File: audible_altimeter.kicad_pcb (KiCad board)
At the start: 2 copper layers, 52.4 x 29.3 mm, 77 parts, among them CON1 BUQ2-USB-MICRO-B, IC1 BUQ2-ATXMEGA128A4U-A, P1 CONN_2, Q1 NPN, SW1 SW_LEFT, SW2 SW_DOWN, SW3 SW_UP, SW4 SW_CENTER, SW5 SW_RIGHT, U1 MCP7940M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

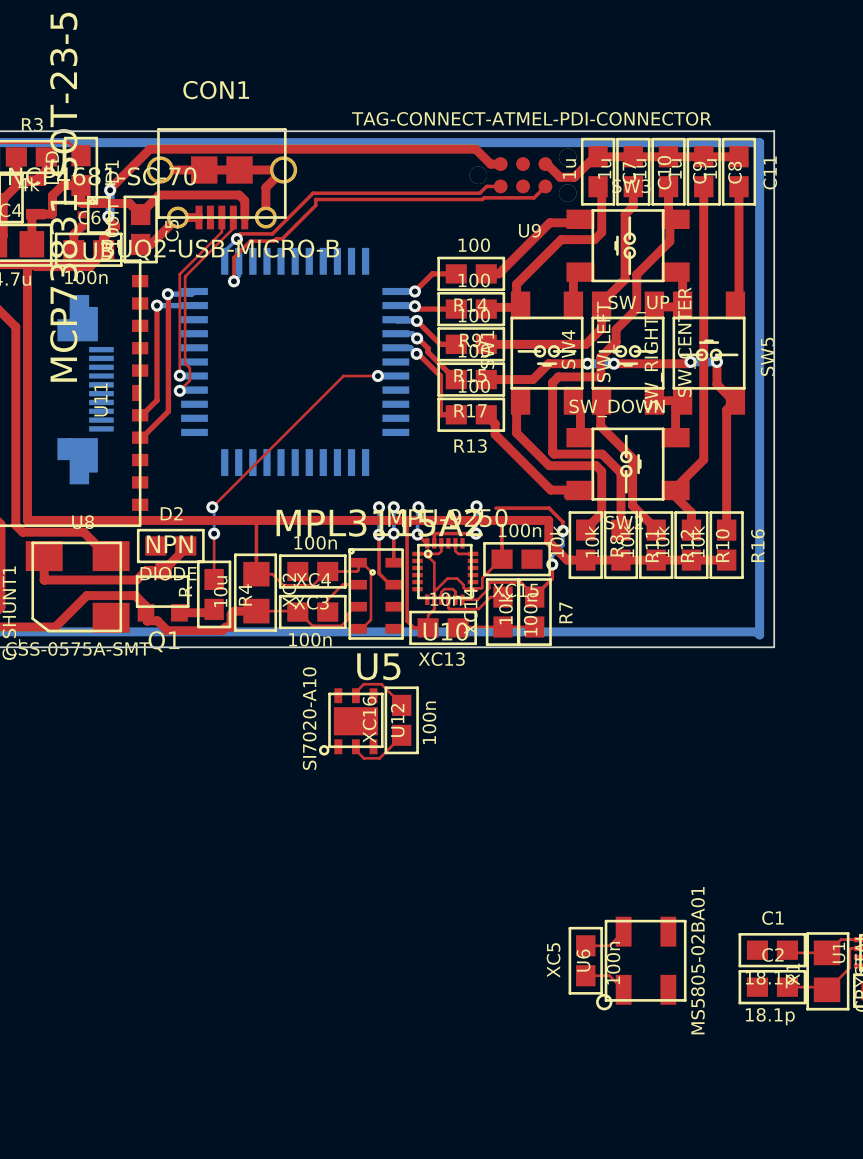
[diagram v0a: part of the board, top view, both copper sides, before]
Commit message: Before making larger board. - Changed GPS module
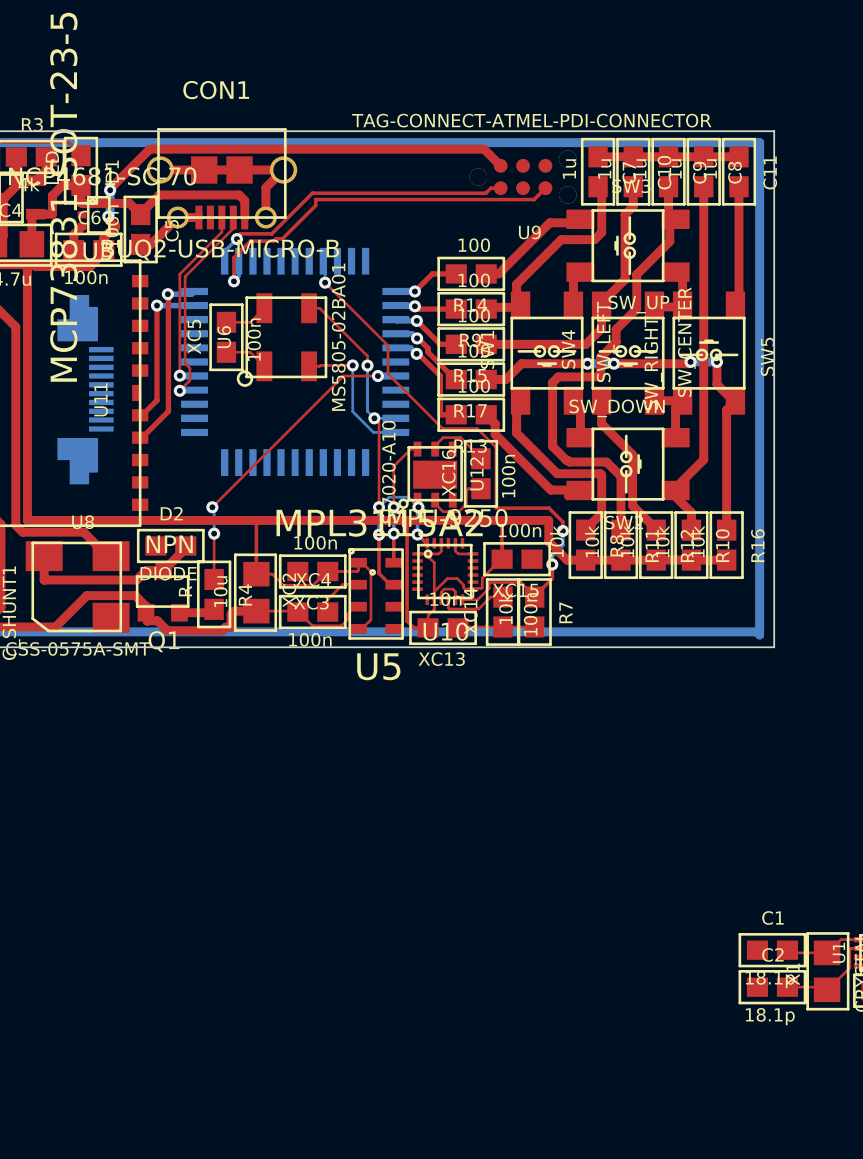
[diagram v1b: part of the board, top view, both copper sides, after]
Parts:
- moved XC5 40.9 mm to (120.9, 34.1)
- moved U6 40.9 mm to (124.3, 34.1)
- moved U12 14.7 mm to (132.8, 42.0)
- moved XC16 14.7 mm to (135.3, 41.9)
- moved U9 0.10 mm to (135.2, 25.0)
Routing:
- net /MCU/ACCELERATOR_INT: track 14.0 -> 33.3 mm, vias 2 -> 3
- net /9-Axis/I2C_SDA: track 7.19 -> 24.4 mm, vias 4 -> 6
- net /9-Axis/I2C_SCL: track 7.61 -> 15.3 mm, vias 4 -> 3
- net GND: track 265.7 -> 262.6 mm

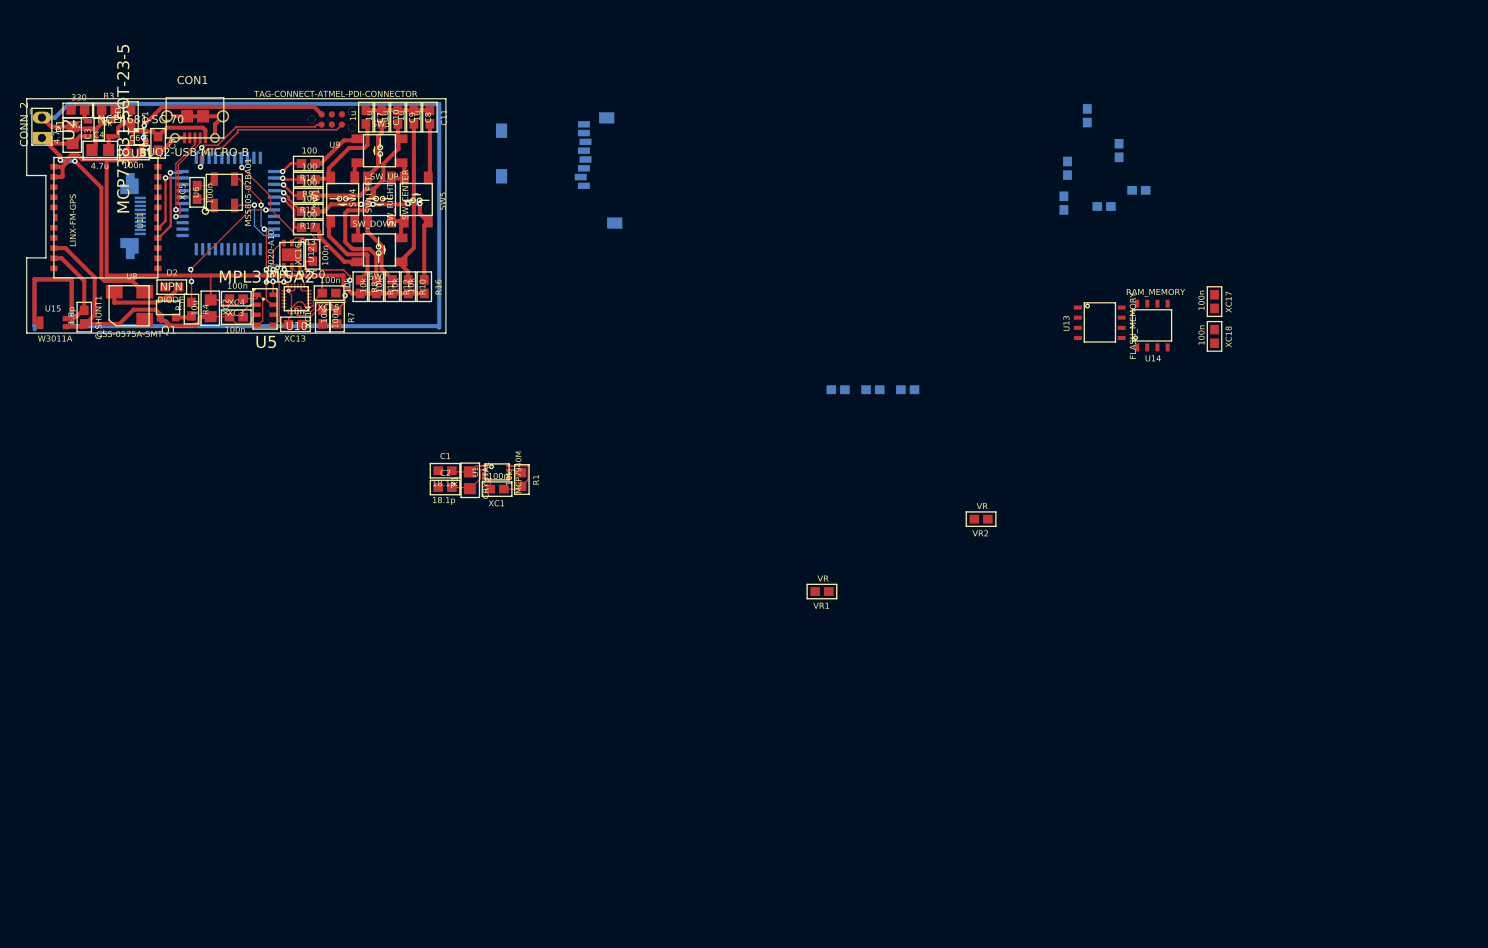
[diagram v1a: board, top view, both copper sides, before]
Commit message: Before adding proper reset and battery monitor
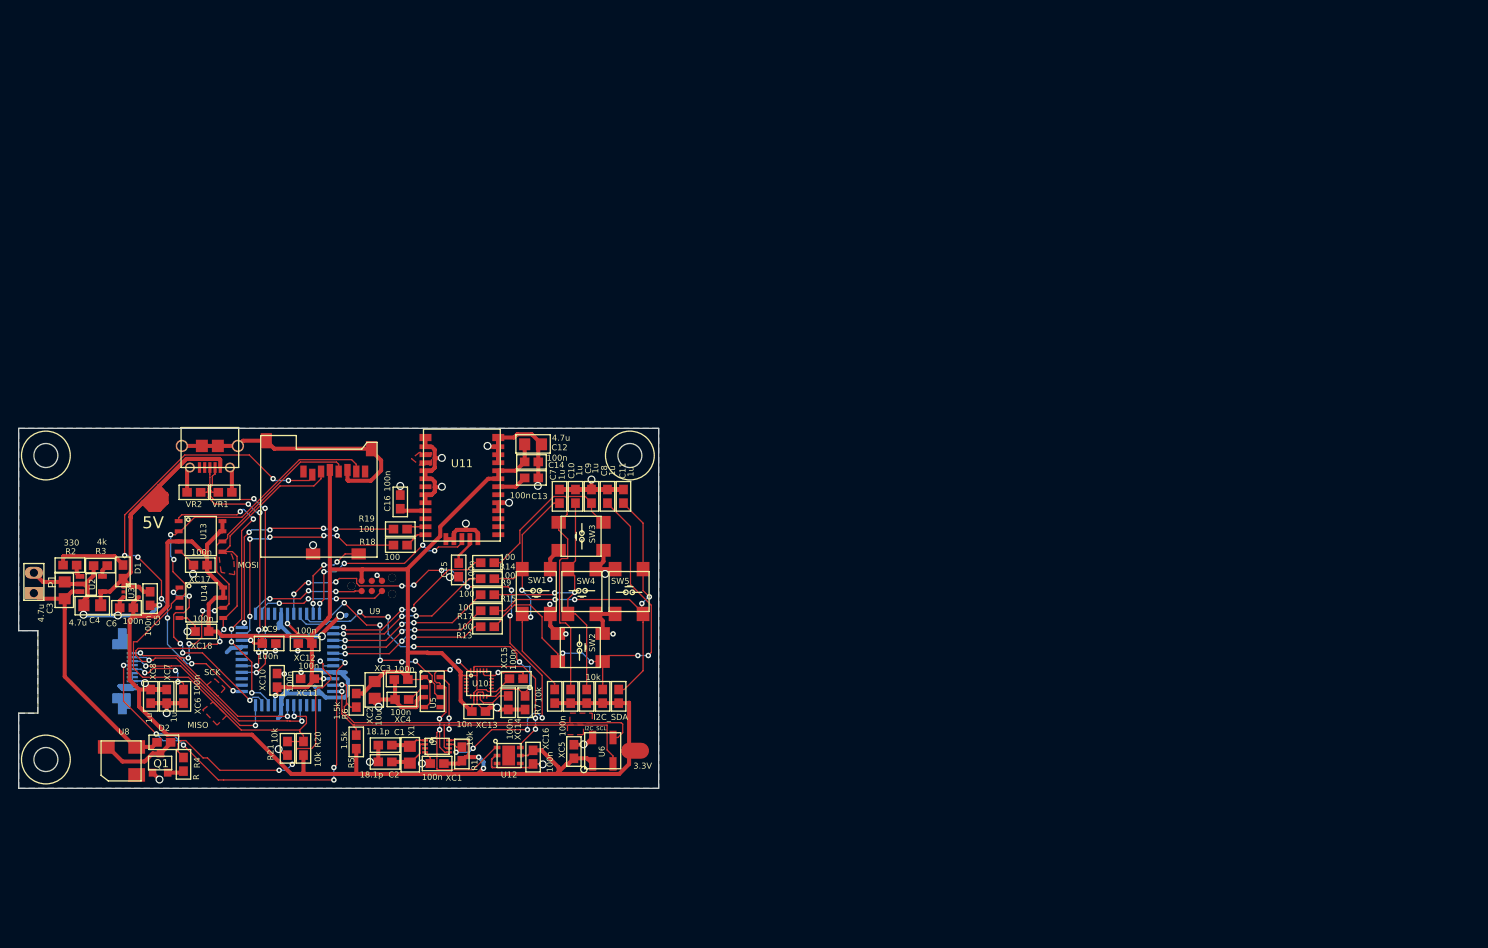
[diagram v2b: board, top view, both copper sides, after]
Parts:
- removed C_SHUNT1: 1.8p, buq2:SM0603
- removed U15: W3011A, buq2:W3011A
- added C12: 4.7u, buq2:SM0805, F.Cu at (162.9, 65.6)
- added C13: 100n, buq2:SM0603, F.Cu at (162.7, 67.8)
- added C14: 100n, buq2:SM0603, F.Cu at (162.7, 69.8)
- added C15: 100n, buq2:SM0603, F.Cu at (153.6, 81.3)
- added C16: 100n, buq2:SM0603, F.Cu at (146.3, 72.8)
- added MOUNTING_HOLE: VAL**, buq2:MOUNTING_HOLE, F.Cu at (102.0, 67.0)
- added MOUNTING_HOLE: VAL**, buq2:MOUNTING_HOLE, F.Cu at (102.0, 105.0)
- added MOUNTING_HOLE: VAL**, buq2:MOUNTING_HOLE, F.Cu at (175.0, 67.0)
- added R18: 100, buq2:SM0603, F.Cu at (146.3, 78.2)
- added R19: 100, buq2:SM0603, F.Cu at (146.3, 76.2)
- added R20: 10k, buq2:SM0603, F.Cu at (134.2, 103.6)
- added R21: 10k, buq2:SM0603, F.Cu at (132.2, 103.6)
- R5, R6, U4, XC10, XC11, XC12, XC6, XC7, XC8, XC9: moved to F.Cu
- SW1, SW2, SW3, SW4, SW5: footprint buq2:PUSHBUTTON_4x4_ROTATED -> buq2:PUSHBUTTON_4x4_5x5_ROTATED
- U11: value LINX-FM-GPS -> SIM33ELA; footprint buq2:LINX-FM-GPS -> buq2:SIM33ELA-GPS
- moved XC18 131.8 mm to (121.5, 89.0), turned to 0 degrees
- moved XC17 131.0 mm to (121.3, 80.7), turned to 0 degrees
- moved XC10 123.4 mm to (130.9, 95.1)
- moved U14 123.4 mm to (118.7, 83.5), turned to 270 degrees
- moved R5 120.7 mm to (140.8, 102.8), turned to 90 degrees
- moved XC12 118.6 mm to (134.4, 90.5)
- moved XC9 117.8 mm to (129.9, 90.5)
- moved U13 115.5 mm to (118.6, 75.2)
- moved XC11 114.4 mm to (134.7, 94.9), turned to 0 degrees
- moved R6 108.1 mm to (140.8, 97.6)
- moved VR2 98.5 mm to (120.5, 71.6), turned to 180 degrees
- moved XC6 98.3 mm to (119.2, 97.1), turned to 270 degrees
- moved XC7 96.2 mm to (117.1, 97.1), turned to 270 degrees
- moved XC8 94.1 mm to (115.1, 97.1), turned to 270 degrees
- moved U6 84.3 mm to (171.6, 103.9)
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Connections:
- U11 pad 10: (no net) -> GND
- U11 pad 11: /Battery/+3.3V -> GND
- U11 pad 12: /Battery/+3.3V -> GND
- U11 pad 13: (no net) -> GND
- U11 pad 14: (no net) -> GND
- U11 pad 15: (no net) -> GND
- U11 pad 16: (no net) -> Net-(U11-Pad16)
- U11 pad 17: (no net) -> Net-(U11-Pad16)
- U11 pad 19: Net-(C_SHUNT1-Pad2) -> GND
- U11 pad 20: GND -> (no net)
- U11 pad 3: /MCU/GPS_PULSE_PER_SECOND -> (no net)
- U11 pad 4: /GPS/TX -> GND
- U11 pad 5: /GPS/RX -> GND
- U11 pad 7: (no net) -> Net-(C14-Pad2)
- U11 pad 8: (no net) -> /Battery/+3.3V
- U11 pad 9: (no net) -> /Battery/+3.3V
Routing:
- net /Battery/+3.3V: track 147.5 -> 333.2 mm, vias 2 -> 7
- net /MCU/MISO: track 0.00 -> 81.7 mm, vias 0 -> 3
- net /Display/MOSI: track 0.00 -> 72.0 mm, vias 0 -> 4
- net /MCU/CLOCK_INT: track 1.74 -> 67.3 mm, vias 0 -> 13
- net /MCU/SCK: track 0.00 -> 64.7 mm, vias 0 -> 6
- net /MicroSD/CSn: track 0.00 -> 59.4 mm, vias 0 -> 8
- net /9-Axis/I2C_SCL: track 15.3 -> 73.8 mm, vias 3 -> 5
- net /MCU/DISPLAY_INVERT: track 0.00 -> 56.7 mm, vias 0 -> 6
- net /Battery/+5V: track 17.8 -> 72.3 mm
- net /9-Axis/I2C_SDA: track 24.4 -> 76.8 mm, vias 6 -> 5
- net /MCU/CSn_FLASH: track 0.00 -> 37.6 mm, vias 0 -> 5
- net /MCU/BAROMETER_INT: track 0.00 -> 27.0 mm, vias 0 -> 5
- net /MCU/CSn_RAM: track 0.00 -> 25.4 mm, vias 0 -> 5
- net /MCU/GPS_PULSE_PER_SECOND: track 0.00 -> 25.3 mm, vias 0 -> 5
- net Net-(C8-Pad1): track 28.6 -> 52.0 mm, vias 0 -> 4
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- added copper zone on F.Cu, net /9-Axis/I2C_SCL
- added copper zone on F.Cu, net /9-Axis/I2C_SDA
- added copper zone on F.Cu, net /Display/MOSI
- added copper zone on F.Cu, net /MCU/MISO
- added copper zone on F.Cu, net /MCU/SCK
- added copper zone on B.Cu, net GND
- added copper zone on F.Cu, net Net-(U11-Pad16)
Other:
- board size 52.4 x 29.3 mm -> 80 x 45 mm
- board text added: "3.3V"
- board text added: "5V"
- board text added: "I2C_SCL"
- board text added: "I2C_SDA"
- board text added: "MISO"
- board text added: "MOSI"
- board text added: "SCK"

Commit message: V1 version which was ordered
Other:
- board text added: "AudibleA V1.0"

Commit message: Start planning test board v2.0
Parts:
- removed C10, C11, C7, C8, C9: 1u, buq2:SM0603
- removed C12: 4.7u, buq2:SM0805
- removed C13, C14, C15, C16, XC14, XC15, XC16, XC18: 100n, buq2:SM0603
- removed LS013B4DN04-FPC: VAL**, buq2:LS013B4DN04-FPC
- removed the MOUNTING_HOLE at (102.0, 67.0)
- removed the MOUNTING_HOLE at (102.0, 105.0)
- removed the MOUNTING_HOLE at (175.0, 67.0)
- removed R10, R11, R12, R16, R20, R21: 10k, buq2:SM0603
- removed R13, R14, R15, R17, R18, R19, R9: 100, buq2:SM0603
- removed SW1: SW_LEFT, buq2:PUSHBUTTON_4x4_5x5_ROTATED
- removed SW2: SW_DOWN, buq2:PUSHBUTTON_4x4_5x5_ROTATED
- removed SW3: SW_UP, buq2:PUSHBUTTON_4x4_5x5_ROTATED
- removed SW4: SW_CENTER, buq2:PUSHBUTTON_4x4_5x5_ROTATED
- removed SW5: SW_RIGHT, buq2:PUSHBUTTON_4x4_5x5_ROTATED
- removed U12: SI7020-A10, buq2:DFN-6-3X3MM
- removed U14: RAM_MEMORY, buq2:8-SOIC
- removed XC13: 10n, buq2:SM0603
- added MOUNTING_HOLE: VAL**, buq2:MOUNTING_HOLE, F.Cu at (139.0, 122.0)
- added MOUNTING_HOLE: VAL**, buq2:MOUNTING_HOLE, F.Cu at (184.5, 122.0)
- added MOUNTING_HOLE: VAL**, buq2:MOUNTING_HOLE, F.Cu at (184.5, 99.5)
- added MOUNTING_HOLE: VAL**, buq2:MOUNTING_HOLE, F.Cu at (139.0, 99.5)
- IC1: moved to F.Cu
- R4: value R -> 1k
- R7, R8: value 10k -> 25
- U10: value MPU-9250 -> CNT; footprint buq2:24QFN-3MM-3MM -> buq2:PUSHBUTTON_4x4_5x5_ROTATED_4_PIN
- U11: value SIM33ELA -> DWN; footprint buq2:SIM33ELA-GPS -> buq2:PUSHBUTTON_4x4_5x5_ROTATED_4_PIN
- U4: value MICRO-SD-CONN -> UP; footprint buq2:MICRO-SD-CONN-AMPHENOL-PUSH-PUSH -> buq2:PUSHBUTTON_4x4_5x5_ROTATED_4_PIN
- U7: footprint buq2:FPC-CONN-10-FCI-BOTTOM-CONTACTS -> buq2:FPC-CONN-10-FCI-TOP-CONTACTS
- moved R4 159.3 mm to (278.4, 98.7), turned to 0 degrees
- moved D2 158.2 mm to (274.9, 103.7), turned to 0 degrees
- moved Q1 154.2 mm to (270.4, 99.7)
- moved U8 148.4 mm to (261.7, 102.4), turned to 0 degrees
- moved R7 112.3 mm to (274.2, 98.7), turned to 0 degrees
- moved R8 105.5 mm to (270.8, 105.8), turned to 0 degrees
- moved VR2 52.8 mm to (163.0, 103.0), turned to 0 degrees
- moved U11 52.6 mm to (177.5, 118.0), turned to 0 degrees
- moved U4 51.9 mm to (177.5, 111.0)
- moved U9 51.5 mm to (184.5, 109.5), turned to 90 degrees
- moved CON1 50.4 mm to (161.0, 101.0)
- moved C4 48.9 mm to (155.0, 98.5), turned to 90 degrees
- moved R3 47.1 mm to (152.5, 98.5), turned to 90 degrees
- moved VR1 46.7 mm to (159.0, 103.0), turned to 0 degrees
- moved U13 45.9 mm to (136.5, 117.5), turned to 0 degrees
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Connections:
- C5 pad 2: /Battery/+5V -> /Battery/BATTERY
- IC1 pad 10: /9-Axis/I2C_SDA -> /Barometer/I2C_SDA
- IC1 pad 11: /9-Axis/I2C_SCL -> /Barometer/I2C_SCL
- IC1 pad 2: /Buttons/BUTTON_LEFT -> /Buttons/BUTTON_CENTER
- IC1 pad 21: /MCU/CSn_RAM -> /Display/CS
- IC1 pad 22: /Display/CS -> /Display/DISP_ON
- IC1 pad 23: /MicroSD/CSn -> (no net)
- IC1 pad 24: (no net) -> /Buzzer/BUZZER_DRIVE
- IC1 pad 3: /Buttons/BUTTON_CENTER -> /Buttons/BUTTON_DOWN
- IC1 pad 32: /GPS/RX -> (no net)
- IC1 pad 33: /GPS/TX -> (no net)
- IC1 pad 4: /Buttons/BUTTON_RIGHT -> (no net)
- IC1 pad 41: /MCU/ACCELERATOR_INT -> (no net)
- IC1 pad 43: /MicroSD/CARD_DETECT -> (no net)
- IC1 pad 44: /MCU/GPS_PULSE_PER_SECOND -> (no net)
- IC1 pad 5: /Buttons/BUTTON_DOWN -> (no net)
- IC1 pad 6: /MCU/DISPLAY_INVERT -> (no net)
- IC1 pad 7: /Buzzer/BUZZER_DRIVE -> (no net)
- R5 pad 2: /9-Axis/I2C_SCL -> /Barometer/I2C_SCL
- R6 pad 2: /9-Axis/I2C_SDA -> /Barometer/I2C_SDA
- R7 pad 1: GND -> Net-(R7-Pad1)
- R7 pad 2: /MCU/ACCELERATOR_INT -> /Battery/BATTERY
- R8 pad 1: /Battery/+3.3V -> Net-(R8-Pad1)
- R8 pad 2: Net-(C7-Pad1) -> Net-(R7-Pad1)
- U1 pad 5: /9-Axis/I2C_SDA -> /Barometer/I2C_SDA
- U1 pad 6: /9-Axis/I2C_SCL -> /Barometer/I2C_SCL
- U10 pad 1: /Battery/+3.3V -> GND
- U10 pad 4: (no net) -> /Buttons/BUTTON_CENTER
- U11 pad 1: (no net) -> GND
- U11 pad 4: GND -> /Buttons/BUTTON_DOWN
- U3 pad 1: /Battery/+5V -> /Battery/BATTERY
- U3 pad 5: /Battery/+5V -> /Battery/BATTERY
- U4 pad 1: (no net) -> GND
- U4 pad 2: /MicroSD/CSn -> (no net)
- U4 pad 3: /Display/MOSI -> (no net)
- U4 pad 4: /Battery/+3.3V -> /Buttons/BUTTON_UP
- U5 pad 7: /9-Axis/I2C_SDA -> /Barometer/I2C_SDA
- U5 pad 8: /9-Axis/I2C_SCL -> /Barometer/I2C_SCL
- U6 pad 2: /9-Axis/I2C_SCL -> /Barometer/I2C_SCL
- U6 pad 3: /9-Axis/I2C_SDA -> /Barometer/I2C_SDA
- U7 pad 4: /MCU/DISPLAY_INVERT -> GND
- U7 pad 8: /Battery/+3.3V -> GND
- U8 pad 1: /Battery/BATTERY -> Net-(R8-Pad1)
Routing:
- net /Battery/+3.3V: track 333.2 -> 4.58 mm, vias 7 -> 0
- net GND: track 271.0 -> 28.3 mm, vias 39 -> 0
- net /MCU/MISO: track 81.7 -> 0.00 mm, vias 3 -> 0
- net /9-Axis/I2C_SDA: track 76.8 -> 0.00 mm, vias 5 -> 0
- net /9-Axis/I2C_SCL: track 73.8 -> 0.00 mm, vias 5 -> 0
- net /Display/MOSI: track 72.0 -> 0.00 mm, vias 4 -> 0
- net /MCU/CLOCK_INT: track 67.3 -> 0.00 mm, vias 13 -> 0
- net /MCU/SCK: track 64.7 -> 0.00 mm, vias 6 -> 0
- net /MicroSD/CSn: track 59.4 -> 0.00 mm, vias 8 -> 0
- net /MCU/DISPLAY_INVERT: track 56.7 -> 0.00 mm, vias 6 -> 0
- net Net-(C8-Pad1): track 52.0 -> 0.00 mm, vias 4 -> 0
- net /Battery/+5V: track 72.3 -> 22.2 mm
- net Net-(C9-Pad1): track 46.9 -> 0.00 mm
- net Net-(C11-Pad1): track 46.8 -> 0.00 mm, vias 4 -> 0
- net /MCU/ACCELERATOR_INT: track 45.1 -> 0.00 mm, vias 5 -> 0
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- removed copper zone on F.Cu, net /9-Axis/I2C_SCL
- removed copper zone on F.Cu, net /9-Axis/I2C_SDA
- removed copper zone on F.Cu, net /Display/MOSI
- removed copper zone on F.Cu, net /MCU/MISO
- removed copper zone on F.Cu, net /MCU/SCK
- removed copper zone on B.Cu, net GND
- removed copper zone on F.Cu, net Net-(U11-Pad16)
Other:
- board size 80 x 45 mm -> 52 x 29 mm
- board text removed: "3.3V"
- board text removed: "5V"
- board text removed: "AudibleA V1.0"
- board text removed: "I2C_SCL"
- board text removed: "I2C_SDA"
- board text removed: "MISO"
- board text removed: "MOSI"
- board text removed: "SCK"

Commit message: Almost ready routing
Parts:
- added LS013B7DH03-FPC: VAL**, buq2:LS013B7DH03-FPC, F.Cu at (138.8, 142.5)
- added SP1: SPEAKER, buq2:SPEAKER_240326000031, F.Cu at (170.0, 103.5)
- moved R4 113.6 mm to (165.0, 106.0), turned to 270 degrees
- moved Q1 100.2 mm to (171.0, 112.0)
- moved D2 100.0 mm to (175.0, 100.5), turned to 90 degrees
- moved R8 95.1 mm to (176.0, 97.5)
- moved R7 94.2 mm to (180.0, 97.5)
- moved U8 94.2 mm to (167.5, 101.5)
- moved R1 20.2 mm to (174.0, 116.0)
- moved C2 20.1 mm to (166.0, 115.0), turned to 270 degrees
- moved U1 19.3 mm to (170.0, 118.5)
- moved X1 19.3 mm to (168.5, 117.0)
- moved XC1 19.0 mm to (174.2, 118.9)
- moved C1 18.8 mm to (165.0, 118.0)
- moved XC7 8.61 mm to (146.5, 108.6)
- moved U4 8.14 mm to (179.0, 103.0), turned to 90 degrees
- moved R6 7.78 mm to (163.0, 122.5)
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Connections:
- IC1 pad 1: /Buttons/BUTTON_UP -> (no net)
- IC1 pad 12: (no net) -> /Buttons/BUTTON_DOWN
- IC1 pad 13: (no net) -> /Buttons/BUTTON_CENTER
- IC1 pad 14: (no net) -> /Buttons/BUTTON_UP
- IC1 pad 2: /Buttons/BUTTON_CENTER -> (no net)
- IC1 pad 20: /MCU/CSn_FLASH -> (no net)
- IC1 pad 21: /Display/CS -> (no net)
- IC1 pad 22: /Display/DISP_ON -> (no net)
- IC1 pad 3: /Buttons/BUTTON_DOWN -> (no net)
- IC1 pad 40: /MCU/CLOCK_INT -> (no net)
- IC1 pad 42: /MCU/BAROMETER_INT -> /Display/DISP_ON
- IC1 pad 43: (no net) -> /Display/CS
- IC1 pad 44: (no net) -> /MCU/CSn_FLASH
- IC1 pad 6: (no net) -> /MCU/CLOCK_INT
- IC1 pad 7: (no net) -> /MCU/BAROMETER_INT
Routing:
- net /Battery/+3.3V: track 4.58 -> 145.9 mm, vias 0 -> 15
- net /Barometer/I2C_SDA: track 0.00 -> 61.7 mm, vias 0 -> 2
- net /Battery/BATTERY: track 13.1 -> 66.3 mm
- net GND: track 28.3 -> 67.3 mm, vias 0 -> 15
- net /MCU/PDI_DATA: track 0.00 -> 38.9 mm, vias 0 -> 6
- net /MCU/PDI_CLK: track 0.00 -> 36.8 mm, vias 0 -> 6
- net /Barometer/I2C_SCL: track 0.00 -> 35.5 mm
- net /Display/MOSI: track 0.00 -> 28.1 mm, vias 0 -> 3
- net /MCU/BAROMETER_INT: track 0.00 -> 26.2 mm, vias 0 -> 4
- net /Buttons/BUTTON_DOWN: track 0.00 -> 25.3 mm
- net /MCU/MISO: track 0.00 -> 25.2 mm
- net /MCU/SCK: track 0.00 -> 24.5 mm, vias 0 -> 4
- net /MCU/CLOCK_INT: track 0.00 -> 22.7 mm
- net /Buttons/BUTTON_UP: track 0.00 -> 17.9 mm, vias 0 -> 2
- net /Buttons/BUTTON_CENTER: track 0.00 -> 16.9 mm, vias 0 -> 2
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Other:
- outline, holes or cut-outs redrawn
